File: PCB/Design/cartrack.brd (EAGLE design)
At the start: 100 x 80 mm, 1 part

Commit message: Done most of the GSM schematic.
Power and GPS remain
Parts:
- added C1: 1uF, resistor:C0603
- added LED1: (no value), led:SML0603
- added Q1, Q2: (no value), semicon-smd-ipc:SOT23W
- added R1, R2, R3: 22R, resistor:R0603
- added R4, R5, R6, R7: 4k7, resistor:R0603
- added R8: 300, resistor:R0603
- added U$3: SIMHOLDER, SparkFun-Connectors:SIMHOLDER
- added U$4: SMF05C, Simplex-DiscreteSemi:SC-88
- added U1: ATMEGA644P-20AU, Atmel_By_element14_Batch_1:QFP80P1200X1200X120-44N
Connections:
- new net +2V8: U$1.VDD_EXT, U1.17, U1.27, U1.38, U1.5
- new net +4V: LED1.A, U$1.VBAT1, U$1.VBAT2, U$1.VBAT3
- new net 0V: C1.2, R5.1, R7.1, U$1.AGND, U$1.GND1, U$1.GND2, U$1.GND3, U$1.GND4, U$1.GND5, U$1.GND6, U$1.GND7, U$1.GND8, U$3.C5, U$4.2, U1.18, U1.28, U1.39, U1.6
- new net GSM_PWR: Q1.2, U$1.PWRKEY
- new net GSM_RX: U$1.RXD, U1.12
- new net GSM_STATUS: U$1.STATUS, U1.14
- new net GSM_TX: U$1.TXD, U1.11
- new net N$1: R1.1, U$3.C7, U$4.1
- new net N$10: LED1.C, R8.2
- new net N$2: R2.2, U$3.C3, U$4.6
- new net N$3: R3.2, U$3.C2, U$4.4
- new net N$4: Q1.3, R5.2
- new net N$5: Q1.1, R4.2
- new net N$6: R4.1, U1.13
- new net N$7: Q2.3, R7.2
- new net N$8: Q2.1, R6.2
- new net N$9: Q2.2, R8.1
- new net NETLIGHT: R6.1, U$1.NETLIGHT
- new net SIM_CLK: R2.1, U$1.SIM_CLK
- new net SIM_DATA: R1.2, U$1.SIM_DATA
- new net SIM_RST: R3.1, U$1.SIM_RST
- new net SIM_VDD: C1.1, U$1.SIM_VDD, U$3.C1, U$4.3

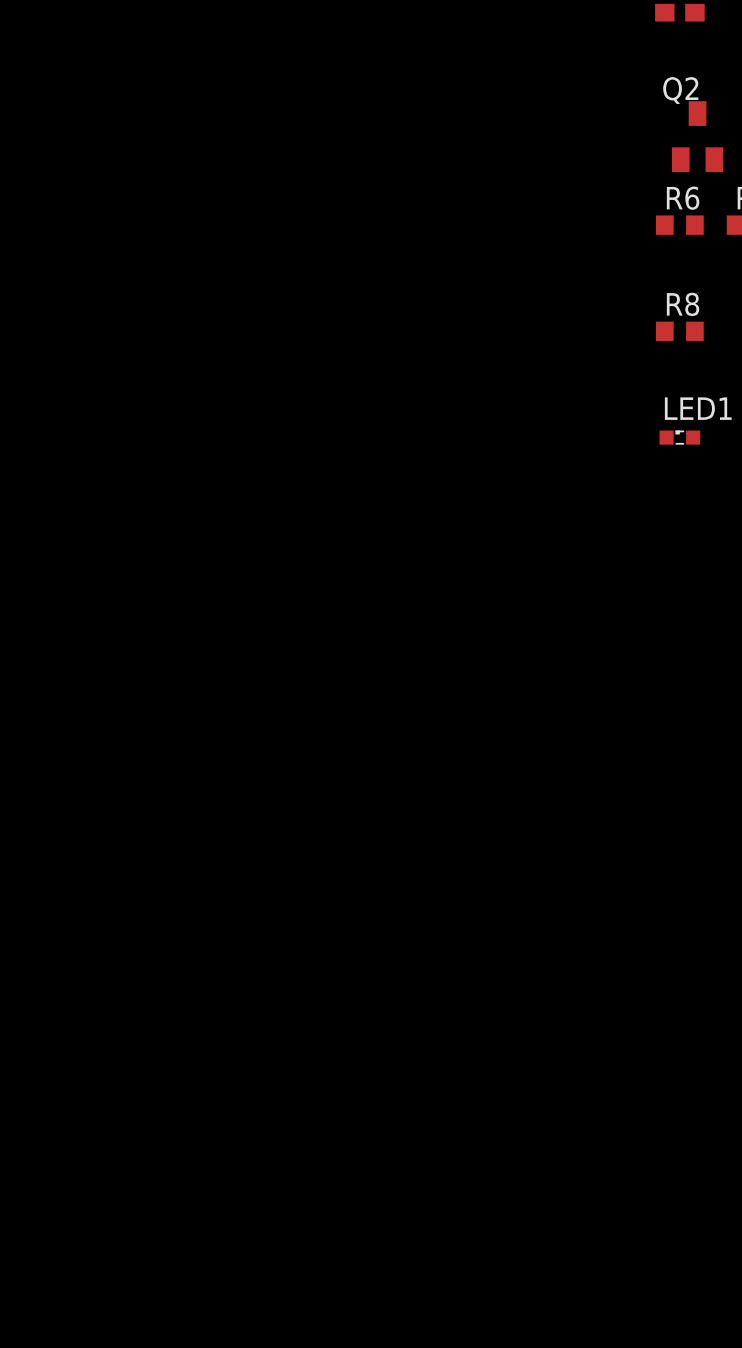
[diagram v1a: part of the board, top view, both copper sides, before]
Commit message: Added GPS to schematic. Need to do power
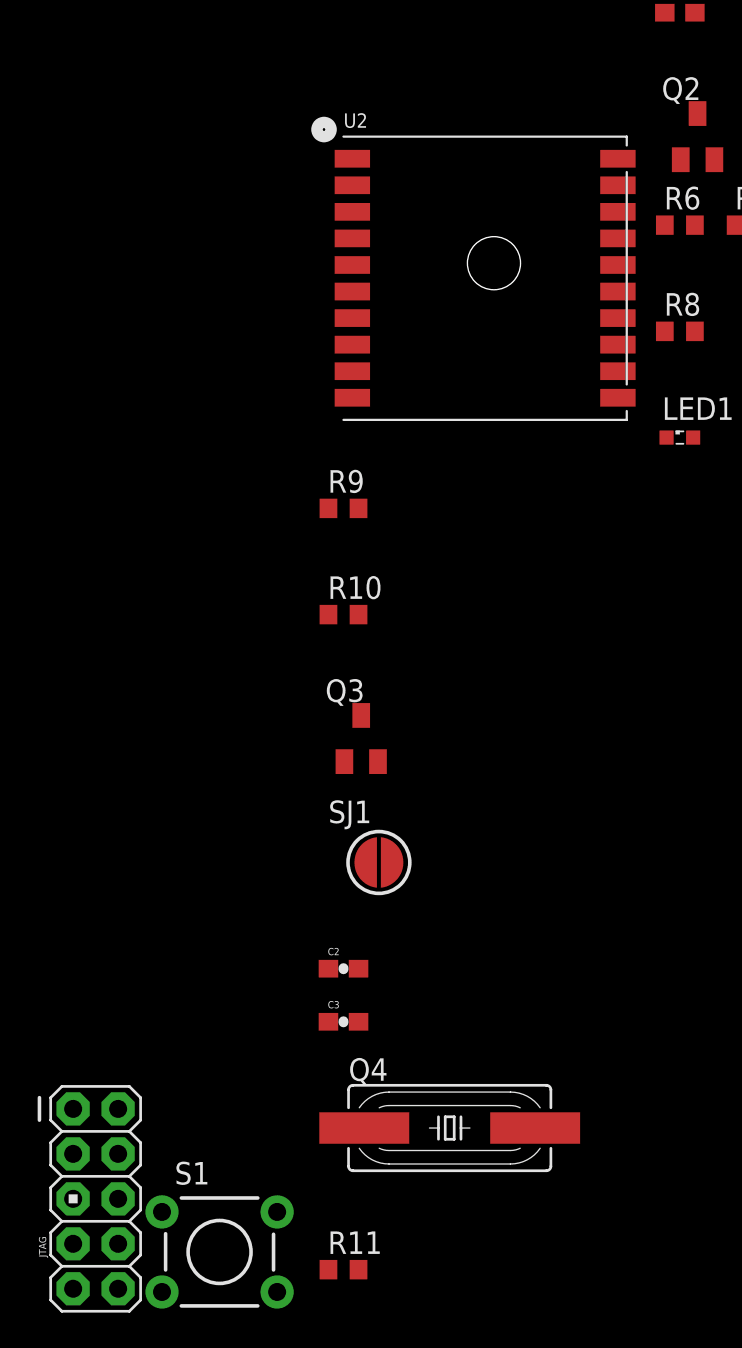
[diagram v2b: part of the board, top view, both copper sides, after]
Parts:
- added C2, C3: 22pF, SparkFun-Passives:0603-CAP
- added JTAG: M05X2PTH, SparkFun-Connectors:AVR_ICSP
- added Q3: (no value), semicon-smd-ipc:SOT23W
- added Q4: 12MHz, crystal:SM49
- added R10, R9: 4k7, resistor:R0603
- added R11: 10k, resistor:R0603
- added S1: SWITCH-MOMENTARY-2PTH, SparkFun-Electromechanical:TACTILE-PTH
- added SJ1: SOLDERJUMPERROUND, SparkFun-Retired:SJ_ROUND
- added U2: (no value), adafruit:FGPMMOPA6H
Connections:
- new net 1PPS: SJ1.2, U2.P$13
- new net GPS_NRESET: Q3.2, U2.P$2
- new net GPS_RESET: R9.1
- new net GPS_RX: U2.P$10
- new net GPS_TX: U2.P$9
- new net N$11: Q3.1, R9.2
- new net N$12: Q3.3, R10.2
- new net N$13: SJ1.1, U1.26
- new net NRESET: JTAG.6, R11.1, S1.3, U1.4
- new net TCK: JTAG.1, U1.21
- new net TDI: JTAG.9, U1.24
- new net TDO: JTAG.3, U1.23
- new net TMS: JTAG.5, U1.22
- new net XTAL1: C3.1, Q4.2, U1.8
- new net XTAL2: C2.1, Q4.1, U1.7
- net +2V8: now also JTAG.4, JTAG.7, R11.2
- net +4V: now also U2.P$1
- net 0V: now also C2.2, C3.2, JTAG.10, JTAG.2, R10.1, S1.1, U2.P$12, U2.P$19, U2.P$3, U2.P$8
- net GSM_RX: now also U1.10
- net GSM_TX: now also U1.9
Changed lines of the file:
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@@
 <element name="R8" library="resistor" package="R0603" value="300" x="-16" y="-82"/>
 <element name="LED1" library="led" package="SML0603" value="" x="-16" y="-88"/>
+<element name="U2" library="adafruit" package="FGPMMOPA6H" value="" x="-27" y="-79"/>
+<element name="R9" library="resistor" package="R0603" value="4k7" x="-35" y="-92"/>
+<element name="R10" library="resistor" package="R0603" value="4k7" x="-35" y="-98"/>
+<element name="Q3" library="semicon-smd-ipc" package="SOT23W" value="" x="-34" y="-105"/>
+<element name="SJ1" library="SparkFun-Retired" package="SJ_ROUND" value="SOLDERJUMPERROUND" x="-33" y="-112"/>
+<element name="C2" library="SparkFun-Passives" package="0603-CAP" value="22pF" x="-35" y="-118"/>
+<element name="C3" library="SparkFun-Passives" package="0603-CAP" value="22pF" x="-35" y="-121"/>
+<element name="Q4" library="crystal" package="SM49" value="12MHz" x="-29" y="-127">
+<attribute name="OC_NEWARK" value="unknown" x="-29" y="-127" size="1.778" layer="27" display="off"/>
+<attribute name="MPN" value="" x="-29" y="-127" size="1.778" layer="27" display="off"/>
+<attribute name="MF" value="" x="-29" y="-127" size="1.778" layer="27" display="off"/>
+<attribute name="OC_FARNELL" value="unknown" x="-29" y="-127" size="1.778" layer="27" display="off"/>
+</element>
+<element name="R11" library="resistor" package="R0603" value="10k" x="-35" y="-135"/>
+<element name="S1" library="SparkFun-Electromechanical" package="TACTILE-PTH" value="SWITCH-MOMENTARY-2PTH" x="-42" y="-134"/>
+<element name="JTAG" library="SparkFun-Connectors" package="AVR_ICSP" value="M05X2PTH" x="-49" y="-131"/>
 </elements>
 <signals>
@@
 <contactref element="R7" pad="1"/>
 <contactref element="U$3" pad="C5"/>
-<wire x1="-15.15" y1="-64" x2="-12.85" y2="-76" width="0" layer="19" extent="1-1"/>
+<contactref element="U2" pad="P$8"/>
+<contactref element="U2" pad="P$3"/>
+<contactref element="U2" pad="P$19"/>
+<contactref element="U2" pad="P$12"/>
+<contactref element="R10" pad="1"/>
+<contactref element="C2" pad="2"/>
+<contactref element="C3" pad="2"/>
+<contactref element="S1" pad="1"/>
+<contactref element="JTAG" pad="2"/>
+<contactref element="JTAG" pad="10"/>
+<wire x1="-45.2512" y1="-131.7394" x2="-47.73" y2="-136.08" width="0" layer="19" extent="1-1"/>
+<wire x1="-47.73" y1="-125.92" x2="-45.2512" y2="-131.7394" width="0" layer="19" extent="1-1"/>
+<wire x1="-34.15" y1="-121" x2="-47.73" y2="-125.92" width="0" layer="19" extent="1-1"/>
+<wire x1="-34.15" y1="-118" x2="-34.15" y2="-121" width="0" layer="19" extent="1-1"/>
+<wire x1="-35.85" y1="-98" x2="-34.15" y2="-118" width="0" layer="19" extent="1-1"/>
+<wire x1="-34.5" y1="-82.75" x2="-35.85" y2="-98" width="0" layer="19" extent="1-1"/>
+<wire x1="-34.5" y1="-75.25" x2="-34.5" y2="-82.75" width="0" layer="19" extent="1-1"/>
+<wire x1="-19.5" y1="-84.25" x2="-34.5" y2="-82.75" width="0" layer="19" extent="1-1"/>
+<wire x1="-19.5" y1="-73.75" x2="-19.5" y2="-84.25" width="0" layer="19" extent="1-1"/>
+<wire x1="-12.85" y1="-76" x2="-19.5" y2="-73.75" width="0" layer="19" extent="1-1"/>
+<wire x1="-15.15" y1="-64" x2="-19.5" y2="-73.75" width="0" layer="19" extent="1-1"/>
 <wire x1="-16.85" y1="-52" x2="-15.15" y2="-64" width="0" layer="19" extent="1-1"/>
 <wire x1="-17" y1="-41.35" x2="-16.85" y2="-52" width="0" layer="19" extent="1-1"/>
@@
 <contactref element="U$1" pad="VBAT3"/>
 <contactref element="LED1" pad="A"/>
-<wire x1="24.69" y1="34.04" x2="-15.25" y2="-88" width="0" layer="19" extent="1-1"/>
+<contactref element="U2" pad="P$1"/>
+<wire x1="-15.25" y1="-88" x2="-34.5" y2="-72.25" width="0" layer="19" extent="1-1"/>
+<wire x1="24.69" y1="34.04" x2="-34.5" y2="-72.25" width="0" layer="19" extent="1-1"/>
 <wire x1="25.99" y1="34.04" x2="24.69" y2="34.04" width="0" layer="19" extent="1-1"/>
 <wire x1="27.29" y1="34.04" x2="25.99" y2="34.04" width="0" layer="19" extent="1-1"/>
@@
 <contactref element="U$1" pad="RXD"/>
 <contactref element="U1" pad="12"/>
-<wire x1="-12.9878" y1="5.2596" x2="12.99" y2="34.04" width="0" layer="19" extent="1-1"/>
+<contactref element="U1" pad="10"/>
+<wire x1="-14.7404" y1="7.7996" x2="12.99" y2="34.04" width="0" layer="19" extent="1-1"/>
+<wire x1="-12.9878" y1="5.2596" x2="-14.7404" y2="7.7996" width="0" layer="19" extent="1-1"/>
 </signal>
 <signal name="GSM_TX">
 <contactref element="U$1" pad="TXD"/>
 <contactref element="U1" pad="11"/>
-<wire x1="-14.7404" y1="7.0122" x2="14.29" y2="34.04" width="0" layer="19" extent="1-1"/>
+<contactref element="U1" pad="9"/>
+<wire x1="-14.7404" y1="8.6124" x2="14.29" y2="34.04" width="0" layer="19" extent="1-1"/>
+<wire x1="-14.7404" y1="7.0122" x2="-14.7404" y2="8.6124" width="0" layer="19" extent="1-1"/>
 </signal>
 <signal name="SIM_VDD">
@@
 <contactref element="U1" pad="17"/>
 <contactref element="U1" pad="5"/>
-<wire x1="-8.2126" y1="16.7404" x2="4.34" y2="24.34" width="0" layer="19" extent="1-1"/>
-<wire x1="-3.2596" y1="10.2126" x2="-8.2126" y2="16.7404" width="0" layer="19" extent="1-1"/>
-<wire x1="-9" y1="5.2596" x2="-3.2596" y2="10.2126" width="0" layer="19" extent="1-1"/>
+<contactref element="R11" pad="2"/>
+<contactref element="JTAG" pad="7"/>
+<contactref element="JTAG" pad="4"/>
+<wire x1="-47.73" y1="-128.46" x2="-50.27" y2="-133.54" width="0" layer="19" extent="1-1"/>
+<wire x1="-34.15" y1="-135" x2="-47.73" y2="-128.46" width="0" layer="19" extent="1-1"/>
+<wire x1="-9" y1="5.2596" x2="-47.73" y2="-128.46" width="0" layer="19" extent="1-1"/>
+<wire x1="-3.2596" y1="10.2126" x2="-9" y2="5.2596" width="0" layer="19" extent="1-1"/>
+<wire x1="-8.2126" y1="16.7404" x2="-3.2596" y2="10.2126" width="0" layer="19" extent="1-1"/>
 <wire x1="-14.7404" y1="11.7874" x2="-8.2126" y2="16.7404" width="0" layer="19" extent="1-1"/>
+<wire x1="4.34" y1="24.34" x2="-8.2126" y2="16.7404" width="0" layer="19" extent="1-1"/>
 </signal>
 <signal name="N$4">
@@
 <wire x1="-15.15" y1="-82" x2="-16.75" y2="-88" width="0" layer="19" extent="1-1"/>
 </signal>
+<signal name="N$11">
+<contactref element="R9" pad="2"/>
+<contactref element="Q3" pad="1"/>
+<wire x1="-34.15" y1="-92" x2="-34.95" y2="-106.303" width="0" layer="19" extent="1-1"/>
+</signal>
+<signal name="N$12">
+<contactref element="Q3" pad="3"/>
+<contactref element="R10" pad="2"/>
+<wire x1="-34.15" y1="-98" x2="-34" y2="-103.697" width="0" layer="19" extent="1-1"/>
+</signal>
+<signal name="GPS_NRESET">
+<contactref element="U2" pad="P$2"/>
+<contactref element="Q3" pad="2"/>
+<wire x1="-34.5" y1="-73.75" x2="-33.05" y2="-106.303" width="0" layer="19" extent="1-1"/>
+</signal>
+<signal name="GPS_RESET">
+<contactref element="R9" pad="1"/>
+</signal>
+<signal name="GPS_TX">
+<contactref element="U2" pad="P$9"/>
+</signal>
+<signal name="GPS_RX">
+<contactref element="U2" pad="P$10"/>
+</signal>
+<signal name="1PPS">
+<contactref element="U2" pad="P$13"/>
+<contactref element="SJ1" pad="2"/>
+<wire x1="-19.5" y1="-82.75" x2="-31.73" y2="-112" width="0" layer="19" extent="1-1"/>
+</signal>
+<signal name="N$13">
+<contactref element="U1" pad="26"/>
+<contactref element="SJ1" pad="1"/>
+<wire x1="-3.2596" y1="9.3998" x2="-34.27" y2="-112" width="0" layer="19" extent="1-1"/>
+</signal>
+<signal name="XTAL2">
+<contactref element="C2" pad="1"/>
+<contactref element="Q4" pad="1"/>
+<contactref element="U1" pad="7"/>
+<wire x1="-35.85" y1="-118" x2="-33.826" y2="-127" width="0" layer="19" extent="1-1"/>
+<wire x1="-14.7404" y1="10.2126" x2="-35.85" y2="-118" width="0" layer="19" extent="1-1"/>
+</signal>
+<signal name="XTAL1">
+<contactref element="Q4" pad="2"/>
+<contactref element="C3" pad="1"/>
+<contactref element="U1" pad="8"/>
+<wire x1="-24.174" y1="-127" x2="-35.85" y2="-121" width="0" layer="19" extent="1-1"/>
+<wire x1="-14.7404" y1="9.3998" x2="-35.85" y2="-121" width="0" layer="19" extent="1-1"/>
+</signal>
+<signal name="NRESET">
+<contactref element="R11" pad="1"/>
+<contactref element="U1" pad="4"/>
+<contactref element="S1" pad="3"/>
+<contactref element="JTAG" pad="6"/>
+<wire x1="-47.73" y1="-131" x2="-45.2512" y2="-136.2606" width="0" layer="19" extent="1-1"/>
+<wire x1="-35.85" y1="-135" x2="-45.2512" y2="-136.2606" width="0" layer="19" extent="1-1"/>
+<wire x1="-14.7404" y1="12.6002" x2="-47.73" y2="-131" width="0" layer="19" extent="1-1"/>
+</signal>
+<signal name="TCK">
+<contactref element="JTAG" pad="1"/>
+<contactref element="U1" pad="21"/>
+<wire x1="-5.7996" y1="5.2596" x2="-50.27" y2="-125.92" width="0" layer="19" extent="1-1"/>
+</signal>
+<signal name="TDO">
+<contactref element="JTAG" pad="3"/>
+<contactref element="U1" pad="23"/>
+<wire x1="-3.2596" y1="7.0122" x2="-50.27" y2="-128.46" width="0" layer="19" extent="1-1"/>
+</signal>
+<signal name="TMS">
+<contactref element="JTAG" pad="5"/>
+<contactref element="U1" pad="22"/>
+<wire x1="-5.0122" y1="5.2596" x2="-50.27" y2="-131" width="0" layer="19" extent="1-1"/>
+</signal>
+<signal name="TDI">
+<contactref element="JTAG" pad="9"/>
+<contactref element="U1" pad="24"/>
+<wire x1="-3.2596" y1="7.7996" x2="-50.27" y2="-136.08" width="0" layer="19" extent="1-1"/>
+</signal>
 </signals>

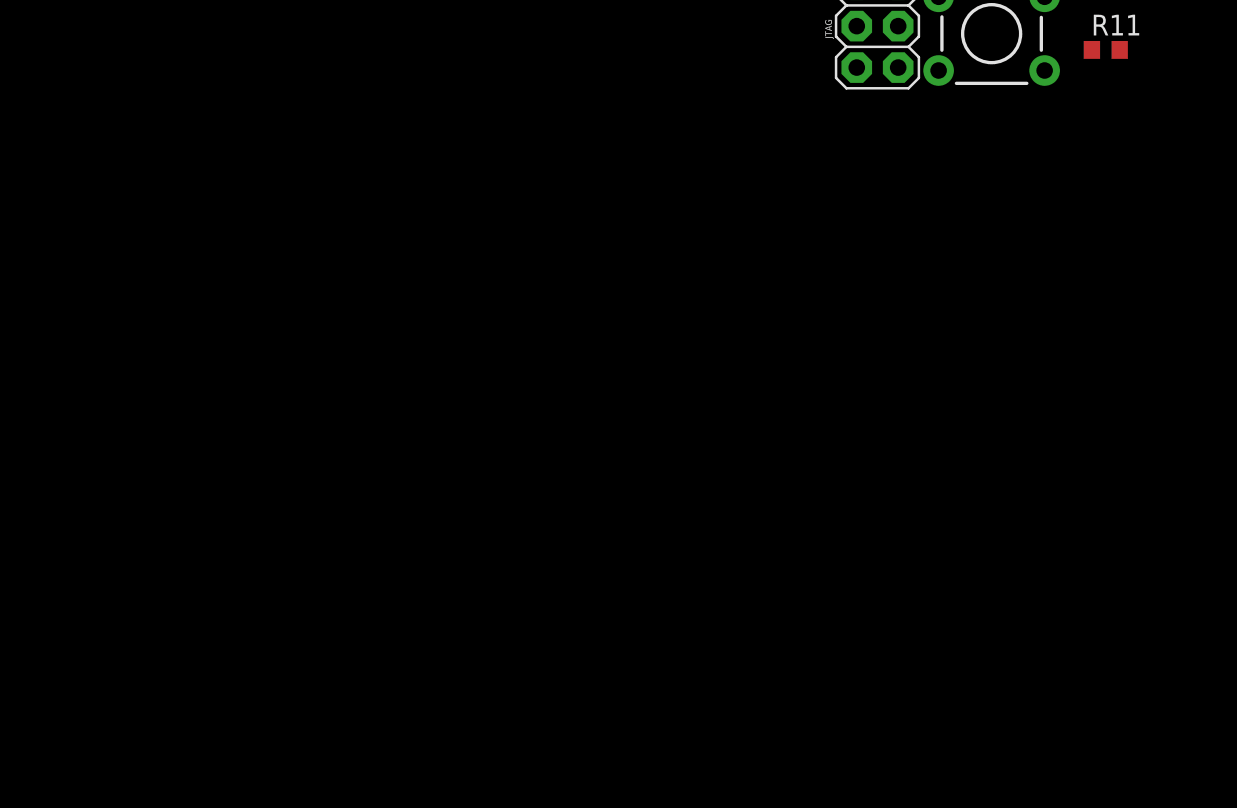
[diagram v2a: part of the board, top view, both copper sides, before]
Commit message: Added all major components to schematic.
Need to do the antenna, decoupling capacitors and layout
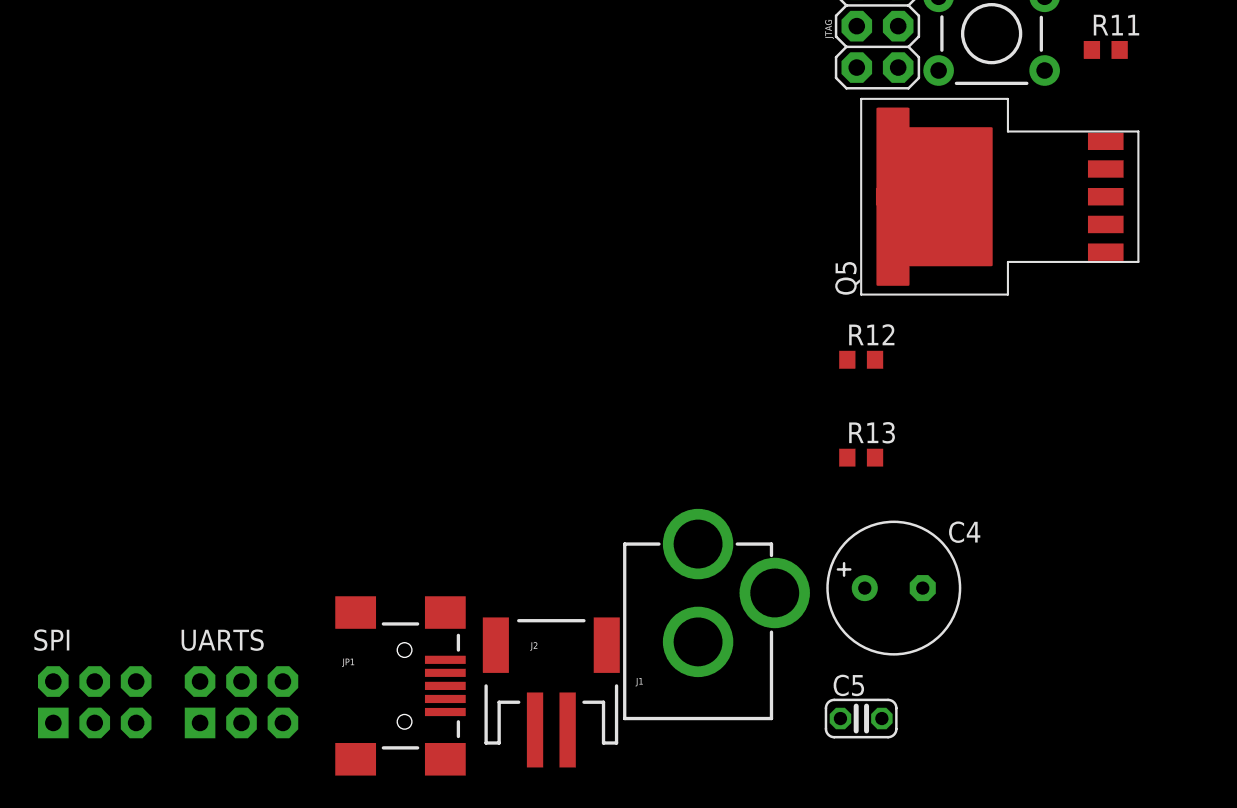
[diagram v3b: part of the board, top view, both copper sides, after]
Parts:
- added C4: 22uF, resistor:E3,5-8
- added C5: 470nF, resistor:C025-024X044
- added J1: POWER_JACKPTH, SparkFun-Connectors:POWER_JACK_PTH
- added J2: (no value), SparkFun-Connectors:JST-2-SMD
- added JP1: USBSMD, SparkFun-Connectors:USB-MINIB
- added Q5: LM2941, misc:LM2941
- added R12: 1k, resistor:R0603
- added R13: 2k2, resistor:R0603
- added SPI, UARTS: (no value), SparkFun-Connectors:2X3-NS
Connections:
- removed net N$12: Q3.3, R10.2
- removed net N$4: Q1.3, R5.2
- new net +5V: C5.1, J1.PWR, J2.2, JP1.VBUS, Q5.VIN
- new net PB4: U1.44
- new net PB5: SPI.4, U1.1
- new net PB6: SPI.1, U1.2
- new net PB7: SPI.3, U1.3
- net +2V8: now also SPI.2
- net +4V: now also C4.+, Q5.VOUT, R13.2
- net 0V: now also C4.-, C5.2, J1.GND, J1.GNDBREAK, J2.1, JP1.GND, Q1.3, Q2.3, Q3.3, Q5.GND, Q5.ONOFF, Q5.TAB, R12.2, SPI.6, UARTS.3, UARTS.4
- net GPS_RESET: now also U1.15
- net GPS_RX: now also U1.10, UARTS.1
- net GPS_TX: now also U1.9, UARTS.2
- net GSM_RX: now also UARTS.5; no longer U1.10
- net GSM_TX: now also UARTS.6; no longer U1.9
- net N$11: now also R10.2
- net N$5: now also R5.2
- net N$7: now also Q5.ADJ, R12.1, R13.1; no longer Q2.3, R7.2
- net N$8: now also R7.2
- net NRESET: now also SPI.5
